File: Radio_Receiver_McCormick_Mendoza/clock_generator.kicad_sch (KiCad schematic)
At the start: 13 parts, among them J10 CLK_2, J11 I_LO, J12 Q_LO, J24 CLK_0, J9 CLK_1, U5 Si5351A-B-GT, U6 74AC74, U7 74AC74, Y2 ASTX-H11-24.576MHZ-T

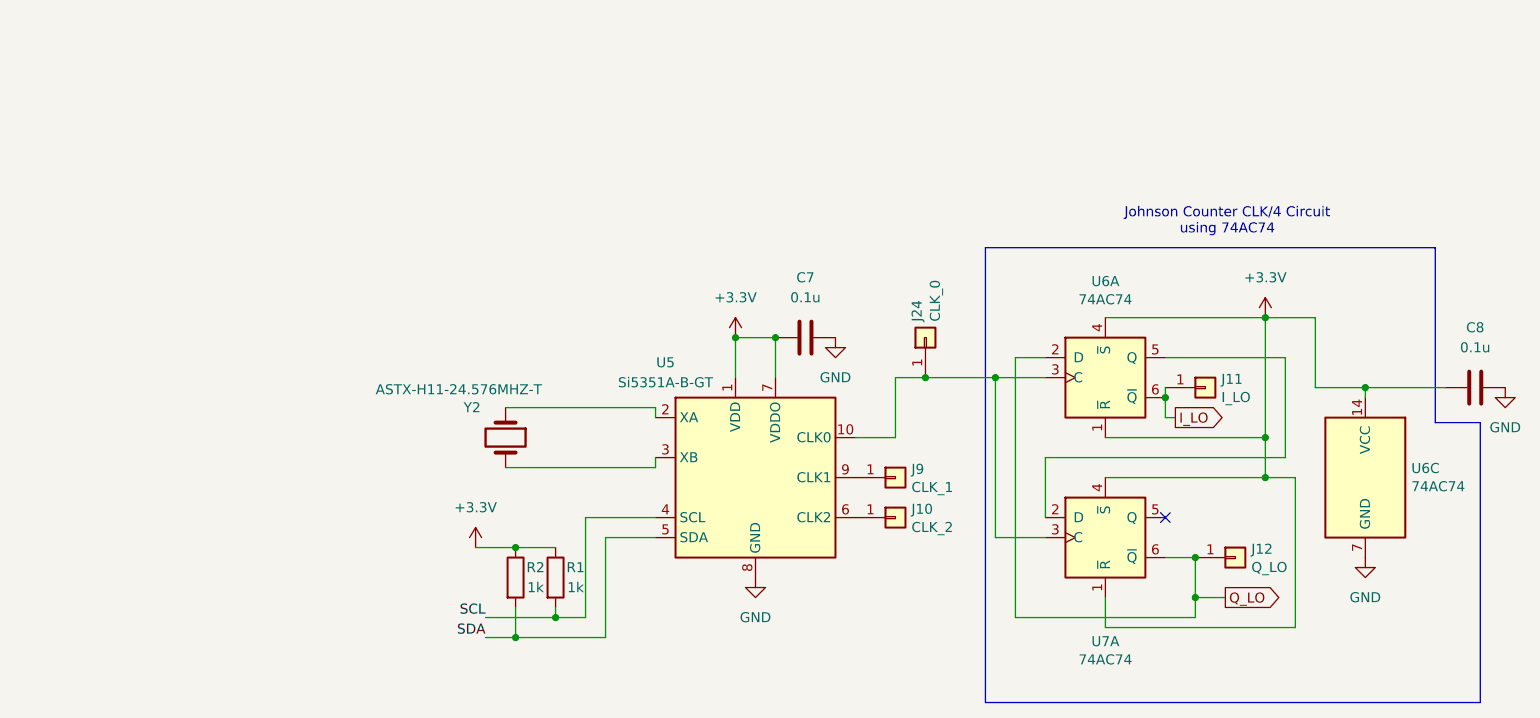
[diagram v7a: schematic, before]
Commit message: Added DAC and shaft angle encoder
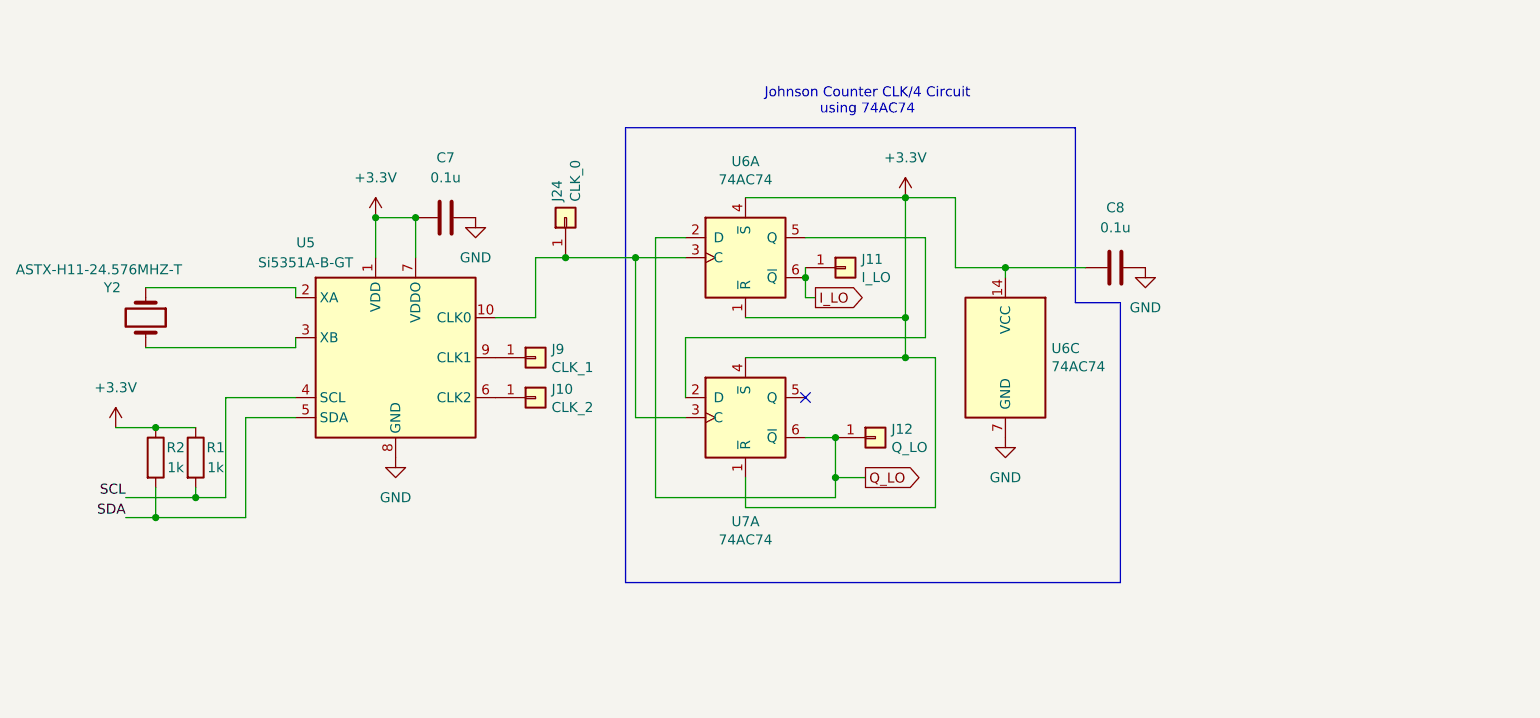
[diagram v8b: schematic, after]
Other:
- moved on the sheet: C7, C8, J10, J11, J12, J24, J9, R1, R2, U5, U6A, U6C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
